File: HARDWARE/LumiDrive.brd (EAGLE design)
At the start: 33 x 57 mm, 88 parts, among them Q1 2.5A/30V/105mΩ, U1 MCP73831, U2 ATSAMD21G-A, U3 3.3V, U4 W25Q32FV, Y1 32.768kHz

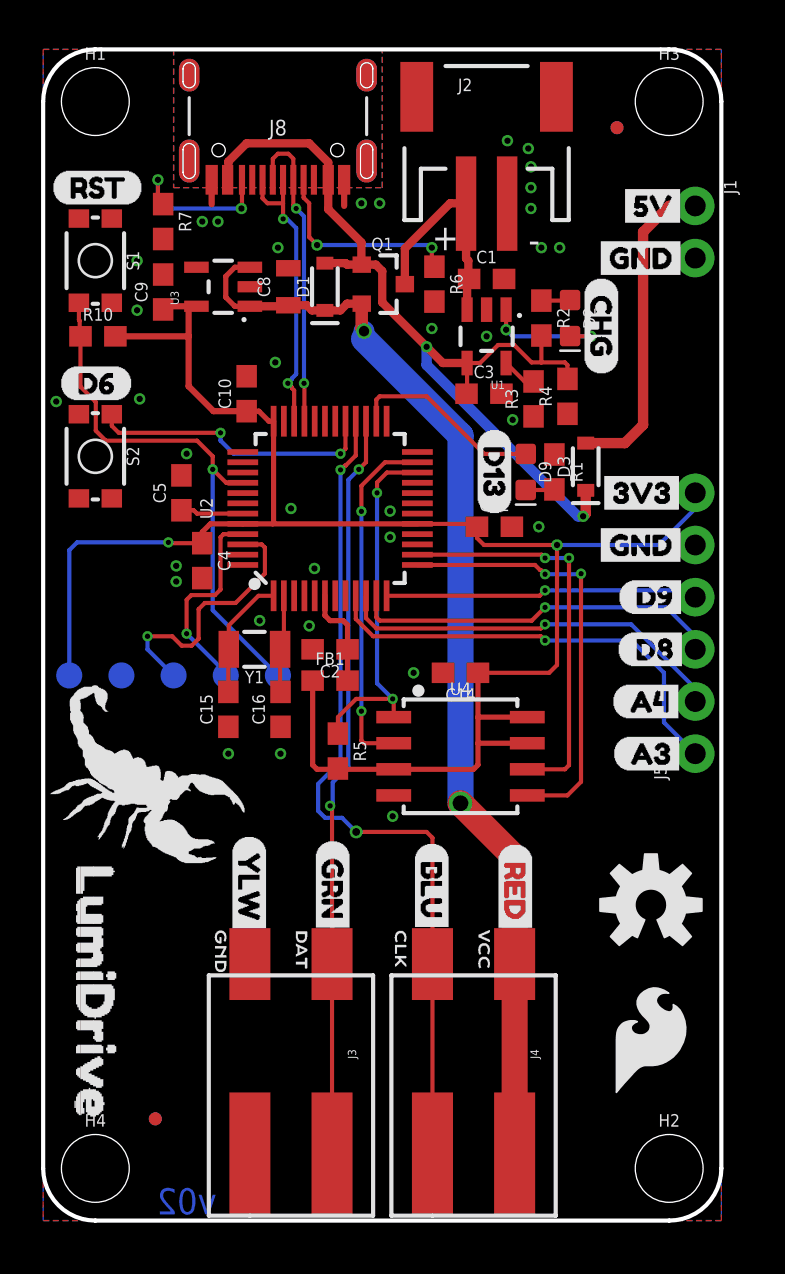
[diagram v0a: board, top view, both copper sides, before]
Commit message: Adds production files and assembly sheet, and fixes swapped lipo connector pads
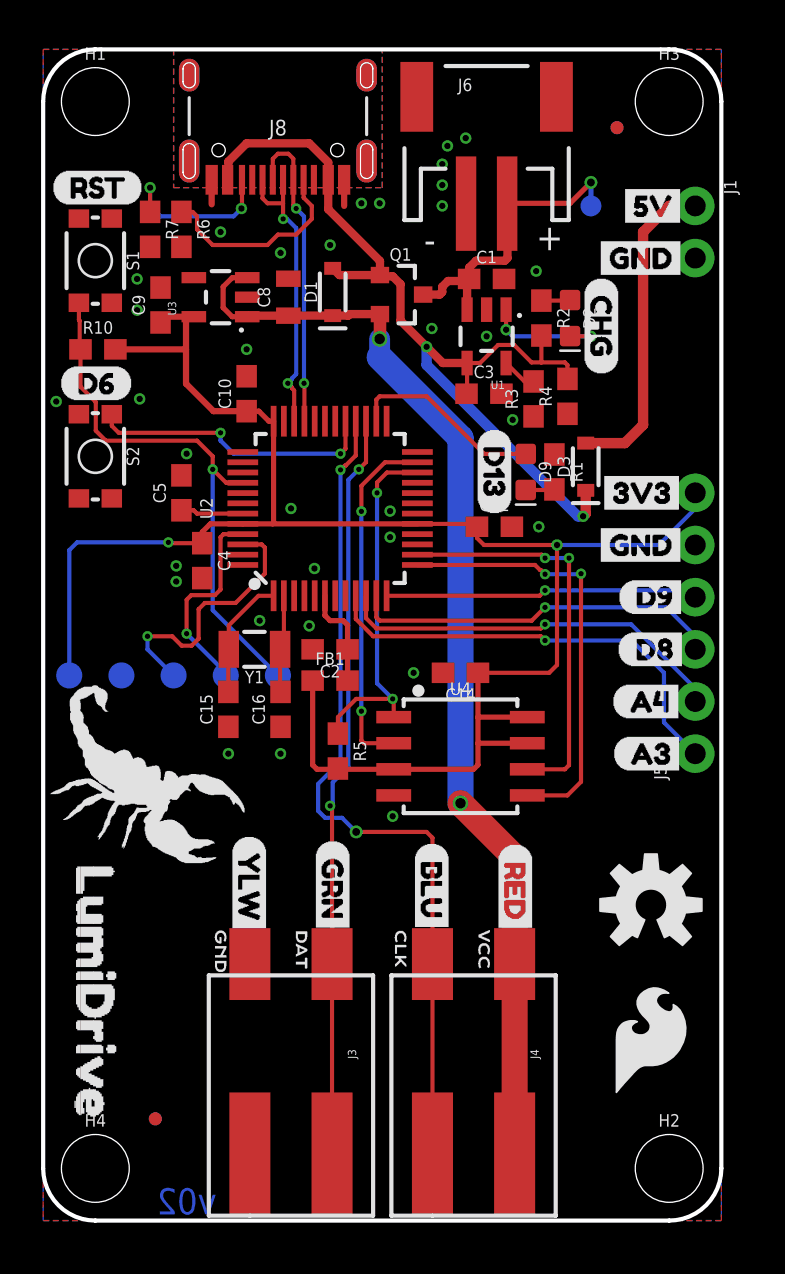
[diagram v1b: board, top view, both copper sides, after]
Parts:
- added TP6: TEST-POINT3X4, SparkFun-Connectors:PAD.03X.04
- moved R6 12.6 mm to (6.73, 48.4)
- moved Q1 1.02 mm to (17.4, 45.2)
- moved R7 0.74 mm to (5.21, 48.4)
- moved C9 0.65 mm to (5.71, 44.7)
- moved R10 0.63 mm to (2.67, 42.5)
- moved U3 0.52 mm to (8.64, 45.1)
- moved C8 0.51 mm to (11.9, 45.1)
- moved D1 0.46 mm to (14.1, 45.3)
- renumbered J2 to J6
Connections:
- net GND: now also J6.1; no longer J6.2
- net V_BATT: now also J6.2, TP6.P$1; no longer J6.1
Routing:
- net V_BATT: track 10.9 -> 15.0 mm, vias 0 -> 1
- net V_USB: track 44.0 -> 44.6 mm
- net 3.3V: track 90.2 -> 89.7 mm
- net N$6: track 10.1 -> 9.99 mm, vias 2 -> 0
- net GND: vias 34 -> 33

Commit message: Adds testpoints to LED SLCK and MOSI lines, extra silk labels for INPUT and OUTPUT .....
 labeling INPUT as 3.3V-5V, deletes old production files
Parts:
- removed U$29: (no value), SCORP_SMALL:SILHOUETTE#OF#A#SCORPION#JPG
- removed U$32: (no value), Labels:5V
- added TP7, TP8: TEST-POINT3X4, SparkFun-Connectors:PAD.03X.04
- added U$25: (no value), OUTPUT:OUTPUT0
- added U$7: (no value), VIN:VIN0
- FB1: device SparkFun-Inductors:0603 -> SparkFun-Coils:0603
- U$6: device LumiDrive_SMALL:LUMIDRIVE0 -> LumiDrive:LUMIDRIVE0
- U$8: device Labels:5V -> VIN_RANGE:3#3#5V0
- U$9: device SCORP_SMALL:SILHOUETTE#OF#A#SCORPION#JPG -> INPUT:INPUT0
- moved U$9 33.4 mm to (27.3, 46.5)
- moved U$6 5.08 mm to (2.54, 24.1)
- moved U$8 3.78 mm to (31.4, 50.8), flipped to the bottom
- moved TP6 2.84 mm to (24.1, 48.3)
- moved J1 1.27 mm to (31.8, 50.8)
- moved U$19 1.27 mm to (26.7, 48.3)
- moved U$26 1.27 mm to (31.5, 48.3)
- moved U3 0.46 mm to (8.89, 44.7)
- moved C8 0.38 mm to (11.9, 44.7)
- moved D1 0.38 mm to (14.1, 45.0)
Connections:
- net LED_MOSI: now also TP7.P$1
- net LED_SCK: now also TP8.P$1
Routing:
- net LED_MOSI: track 36.5 -> 40.4 mm, vias 2 -> 3
- net LED_SCK: track 41.3 -> 45.0 mm, vias 2 -> 3
- net V_BATT: track 15.0 -> 12.2 mm
- net 5V: track 15.6 -> 16.1 mm
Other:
- board text added: "v10"
- board text removed: "v02"

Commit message: Adds clarifying text to the 5V and VIN power symbol, changes silk from "VIN" to "3.3V-5V" , and localizes the "OUTPUT" silk better
- Changes DRC to tight with approval of the drill hit errors for better clarification on design choices
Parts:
- removed U$7: (no value), VIN:VIN0
- added U$29: (no value), VIN_RANGE_SMALL:3#3#5V0
- moved U$25 16.5 mm to (27.4, 37.2)
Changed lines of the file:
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@@
 <layer number="115" name="ReferenceISLANDS" color="7" fill="1" visible="no" active="no"/>
 <layer number="116" name="Patch_BOT" color="9" fill="4" visible="no" active="no"/>
-<layer number="117" name="PM_Ref" color="26" fill="1" visible="no" active="yes"/>
+<layer number="117" name="PM_Ref" color="26" fill="1" visible="yes" active="yes"/>
 <layer number="118" name="Rect_Pads" color="7" fill="1" visible="no" active="no"/>
-<layer number="119" name="PF_Ref" color="31" fill="1" visible="no" active="yes"/>
-<layer number="120" name="WFL_Ref" color="25" fill="1" visible="no" active="yes"/>
+<layer number="119" name="PF_Ref" color="31" fill="1" visible="yes" active="yes"/>
+<layer number="120" name="WFL_Ref" color="25" fill="1" visible="yes" active="yes"/>
 <layer number="121" name="_tsilk" color="7" fill="1" visible="no" active="no"/>
 <layer number="122" name="_bsilk" color="7" fill="1" visible="no" active="no"/>
@@
 </class>
 </classes>
-<designrules name="SparkFun-2-layer-FAB-LIMIT">
+<designrules name="SparkFun-2-layer-TIGHT">
 <description language="en">&lt;b&gt;SparkFun 2 Layer Design Rule Checks - STANDARD/TIGHT/FAB-LIMIT&lt;/b&gt;
 &lt;p&gt;
@@
 <param name="mtCopper" value="0.035mm 0.035mm 0.035mm 0.035mm 0.035mm 0.035mm 0.035mm 0.035mm 0.035mm 0.035mm 0.035mm 0.035mm 0.035mm 0.035mm 0.035mm 0.035mm"/>
 <param name="mtIsolate" value="1.5mm 0.15mm 0.2mm 0.15mm 0.2mm 0.15mm 0.2mm 0.15mm 0.2mm 0.15mm 0.2mm 0.15mm 0.2mm 0.15mm 0.2mm"/>
-<param name="mdWireWire" value="4mil"/>
-<param name="mdWirePad" value="4mil"/>
-<param name="mdWireVia" value="4mil"/>
-<param name="mdPadPad" value="4mil"/>
-<param name="mdPadVia" value="4mil"/>
-<param name="mdViaVia" value="4mil"/>
-<param name="mdSmdPad" value="4mil"/>
-<param name="mdSmdVia" value="4mil"/>
-<param name="mdSmdSmd" value="4mil"/>
+<param name="mdWireWire" value="7mil"/>
+<param name="mdWirePad" value="7mil"/>
+<param name="mdWireVia" value="7mil"/>
+<param name="mdPadPad" value="7mil"/>
+<param name="mdPadVia" value="7mil"/>
+<param name="mdViaVia" value="7mil"/>
+<param name="mdSmdPad" value="7mil"/>
+<param name="mdSmdVia" value="7mil"/>
+<param name="mdSmdSmd" value="7mil"/>
 <param name="mdViaViaSameLayer" value="8mil"/>
 <param name="mnLayersViaInSmd" value="2"/>
-<param name="mdCopperDimension" value="4mil"/>
-<param name="mdDrill" value="4mil"/>
+<param name="mdCopperDimension" value="7mil"/>
+<param name="mdDrill" value="7mil"/>
 <param name="mdSmdStop" value="0mil"/>
-<param name="msWidth" value="4mil"/>
-<param name="msDrill" value="6mil"/>
+<param name="msWidth" value="7mil"/>
+<param name="msDrill" value="15mil"/>
 <param name="msMicroVia" value="9.99mm"/>
 <param name="msBlindViaRatio" value="0.5"/>
@@
 <param name="rvMicroViaOuter" value="0.25"/>
 <param name="rvMicroViaInner" value="0.25"/>
-<param name="rlMinPadTop" value="5mil"/>
+<param name="rlMinPadTop" value="7mil"/>
 <param name="rlMaxPadTop" value="20mil"/>
-<param name="rlMinPadInner" value="6mil"/>
+<param name="rlMinPadInner" value="7mil"/>
 <param name="rlMaxPadInner" value="20mil"/>
-<param name="rlMinPadBottom" value="5mil"/>
+<param name="rlMinPadBottom" value="7mil"/>
 <param name="rlMaxPadBottom" value="20mil"/>
-<param name="rlMinViaOuter" value="5mil"/>
+<param name="rlMinViaOuter" value="7mil"/>
 <param name="rlMaxViaOuter" value="20mil"/>
-<param name="rlMinViaInner" value="6mil"/>
+<param name="rlMinViaInner" value="7mil"/>
 <param name="rlMaxViaInner" value="20mil"/>
 <param name="rlMinMicroViaOuter" value="4mil"/>
@@
 <element name="TP7" library="SparkFun-Connectors" package="PAD.03X.04" value="TEST-POINT3X4" x="12.7" y="8.89" smashed="yes" rot="MR0"/>
 <element name="TP8" library="SparkFun-Connectors" package="PAD.03X.04" value="TEST-POINT3X4" x="17.78" y="8.89" smashed="yes" rot="MR0"/>
-<element name="U$7" library="VIN" package="VIN0" value="" x="27.051" y="50.8" smashed="yes"/>
 <element name="U$8" library="VIN_RANGE" package="3#3#5V0" value="" x="31.369" y="50.8" smashed="yes" rot="MR0"/>
 <element name="U$9" library="INPUT" package="INPUT0" value="" x="27.305" y="46.482" smashed="yes"/>
-<element name="U$25" library="OUTPUT" package="OUTPUT0" value="" x="25.527" y="20.828" smashed="yes"/>
+<element name="U$25" library="OUTPUT" package="OUTPUT0" value="" x="27.432" y="37.211" smashed="yes"/>
 <element name="U$6" library="LumiDrive" package="LUMIDRIVE0" value="" x="2.54" y="24.13" smashed="yes" rot="R270"/>
+<element name="U$29" library="VIN_RANGE_SMALL" package="3#3#5V0" value="" x="26.543" y="50.8" smashed="yes"/>
 </elements>
 <signals>

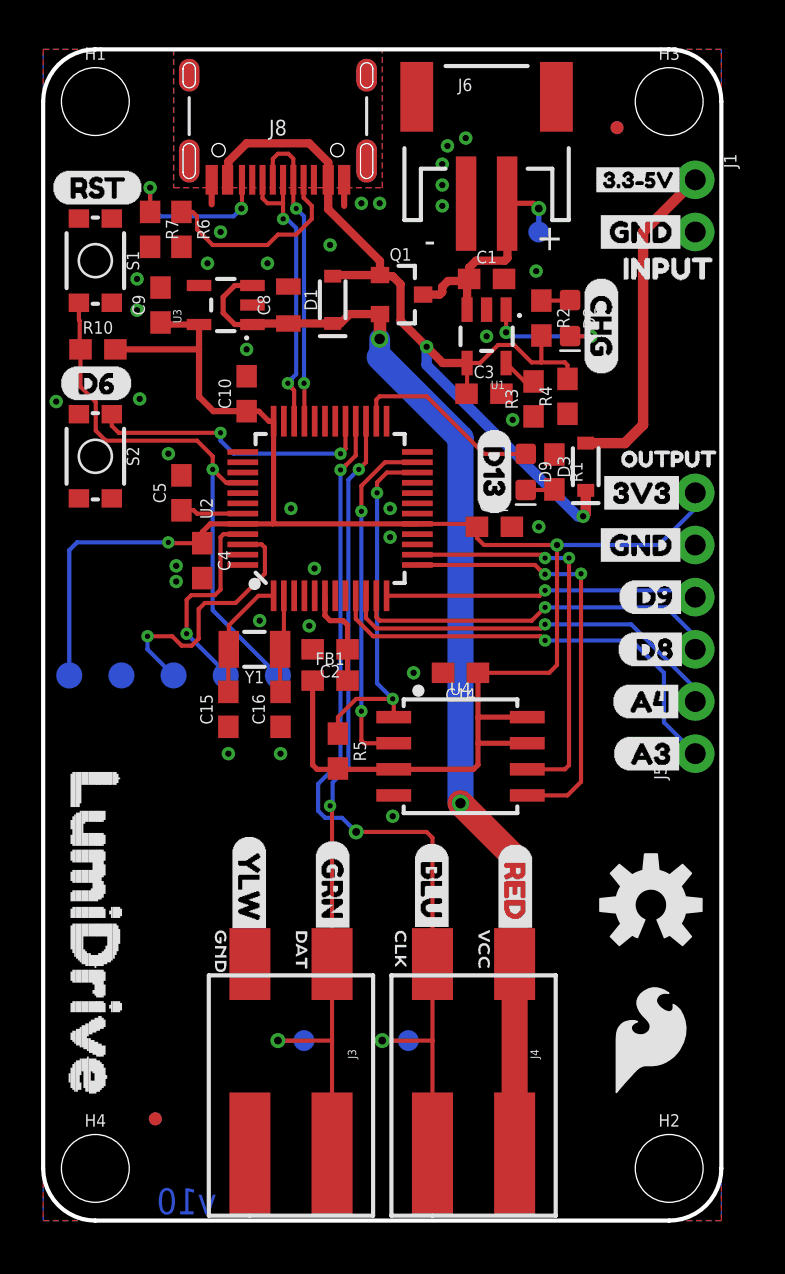
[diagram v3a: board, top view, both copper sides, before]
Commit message: Moves entire design down .005 mils to X-center
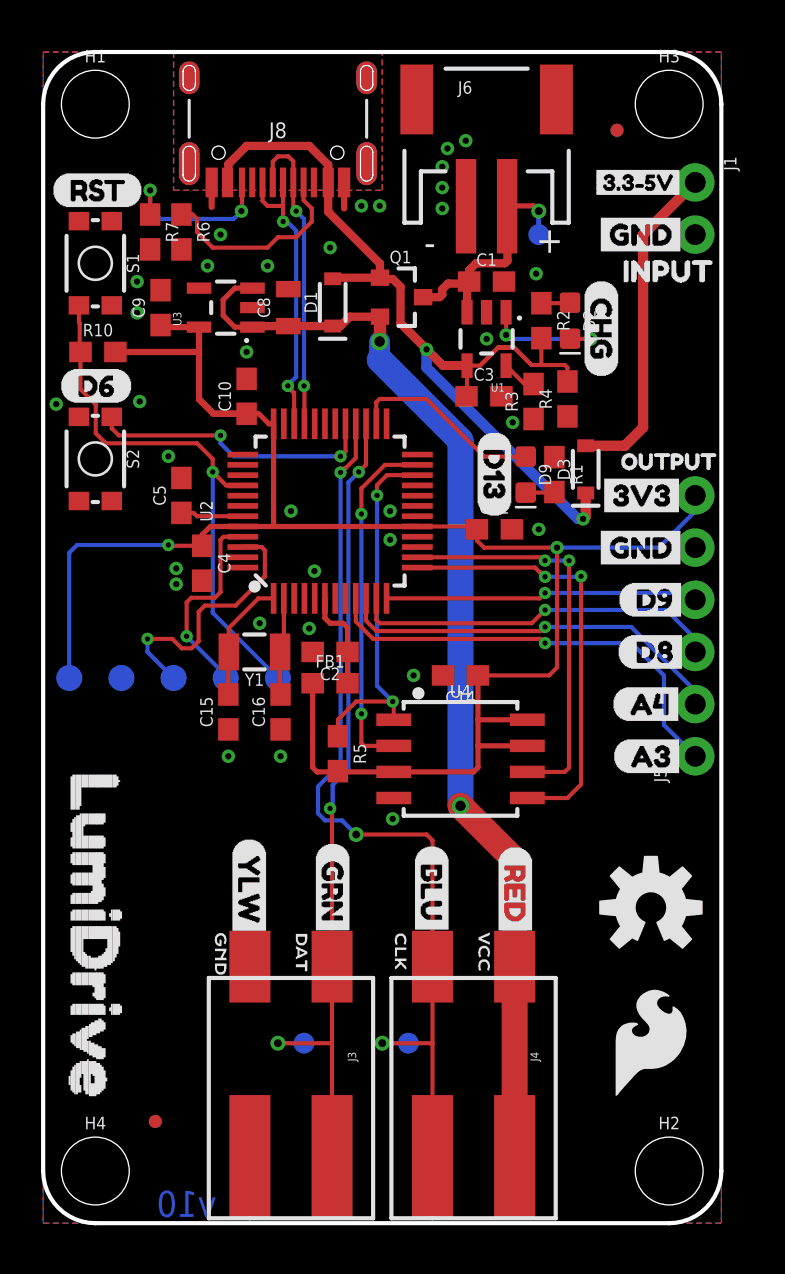
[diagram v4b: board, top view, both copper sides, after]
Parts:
- moved C10 0.13 mm to (9.91, 40.3)
- moved C12 0.13 mm to (22.0, 33.8)
- moved C2 0.13 mm to (14.0, 27.8)
- moved C3 0.13 mm to (21.5, 40.3)
- moved C4 0.13 mm to (7.75, 32.1)
- moved C5 0.13 mm to (6.73, 35.4)
- moved C8 0.13 mm to (11.9, 44.6)
- moved C9 0.13 mm to (5.71, 44.6)
- moved D2 0.13 mm to (25.7, 43.9)
- moved D9 0.13 mm to (23.5, 36.4)
- moved FD1 0.13 mm to (27.9, 53.2)
- moved FD3 0.13 mm to (27.9, 53.2)
- moved H1 0.13 mm to (2.54, 54.5)
- moved H3 0.13 mm to (30.5, 54.5)
- moved J6 0.13 mm to (21.6, 53.2)
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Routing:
- net V_USB: track 44.5 -> 51.8 mm
- net 3.3V: track 90.0 -> 92.6 mm
